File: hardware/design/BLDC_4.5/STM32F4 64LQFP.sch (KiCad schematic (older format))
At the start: 19 parts, among them P2 SWD, U1 STM32F40X_LQFP64, X2 8MHz 10ppm

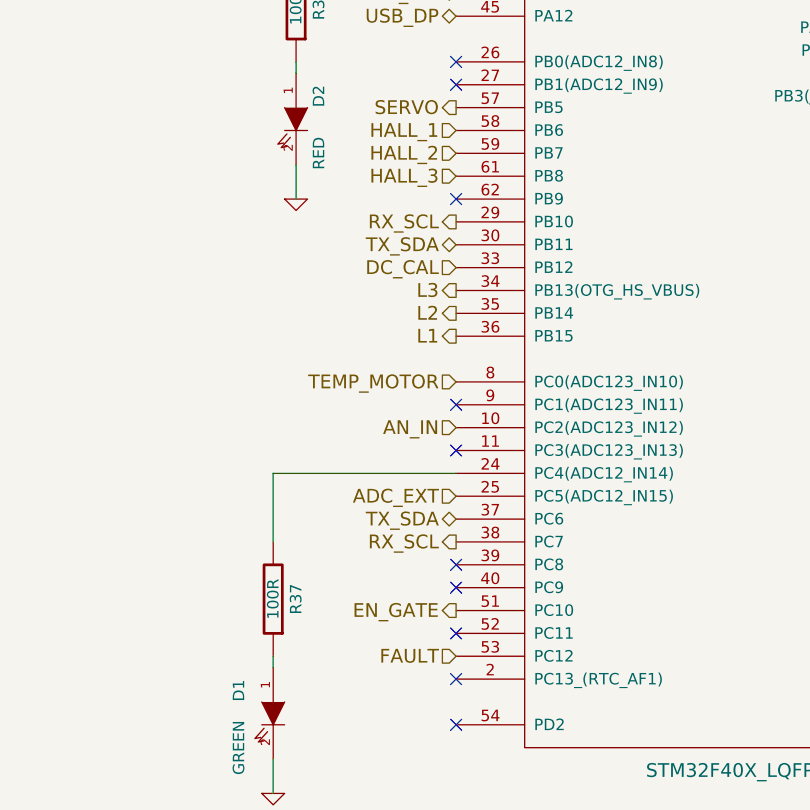
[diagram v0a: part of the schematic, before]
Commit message: Moved HALL_3 to PC11. Added CAN and I2C pullups and temperature sensor to the schematic.
Signed-off-by: Marcos Chaparro <marcos@mrkindustries.com.ar>
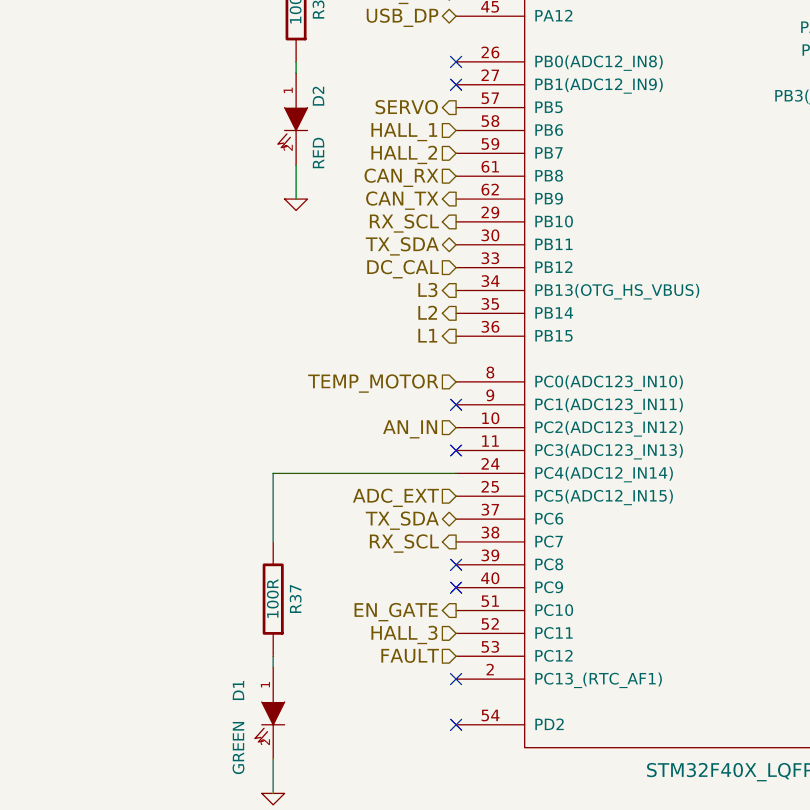
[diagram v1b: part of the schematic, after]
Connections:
- net HALL_3: now also U1.52 (PC11); no longer U1.61 (PB8)
- net CAN_TX: now reaches U1.62 (PB9)
- new net CAN_RX: U1.61 (PB8)
- no-connect marks 19 -> 17
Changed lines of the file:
@@
 LIBS:contrib
 LIBS:valves
+LIBS:mrk-industries
 LIBS:BLDC_4-cache
 EELAYER 24 0
@@
 $Descr A4 11693 8268
 encoding utf-8
-Sheet 3 4
+Sheet 4 6
 Title "BLDC Driver 4.5"
 Date "22 Aug 2014"
@@
 NoConn ~ 4500 5850
 NoConn ~ 4500 5350
-NoConn ~ 4500 3750
 NoConn ~ 4500 3250
 NoConn ~ 4500 3150
 NoConn ~ 4500 5450
-NoConn ~ 4500 5650
 $Comp
 L GND #PWR055
@@
 Text HLabel 4500 3550 0    60   Input ~ 0
 HALL_2
-Text HLabel 4500 3650 0    60   Input ~ 0
+Text HLabel 4500 5650 0    60   Input ~ 0
 HALL_3
 Text HLabel 4500 3850 0    60   Output ~ 0
@@
 Text Notes 9300 1700 0    40   ~ 0
 Bypass, place next to VDD pins
+Text HLabel 4500 3650 0    60   Input ~ 0
+CAN_RX
+Text HLabel 4500 3750 0    60   Output ~ 0
+CAN_TX
 $EndSCHEMATC

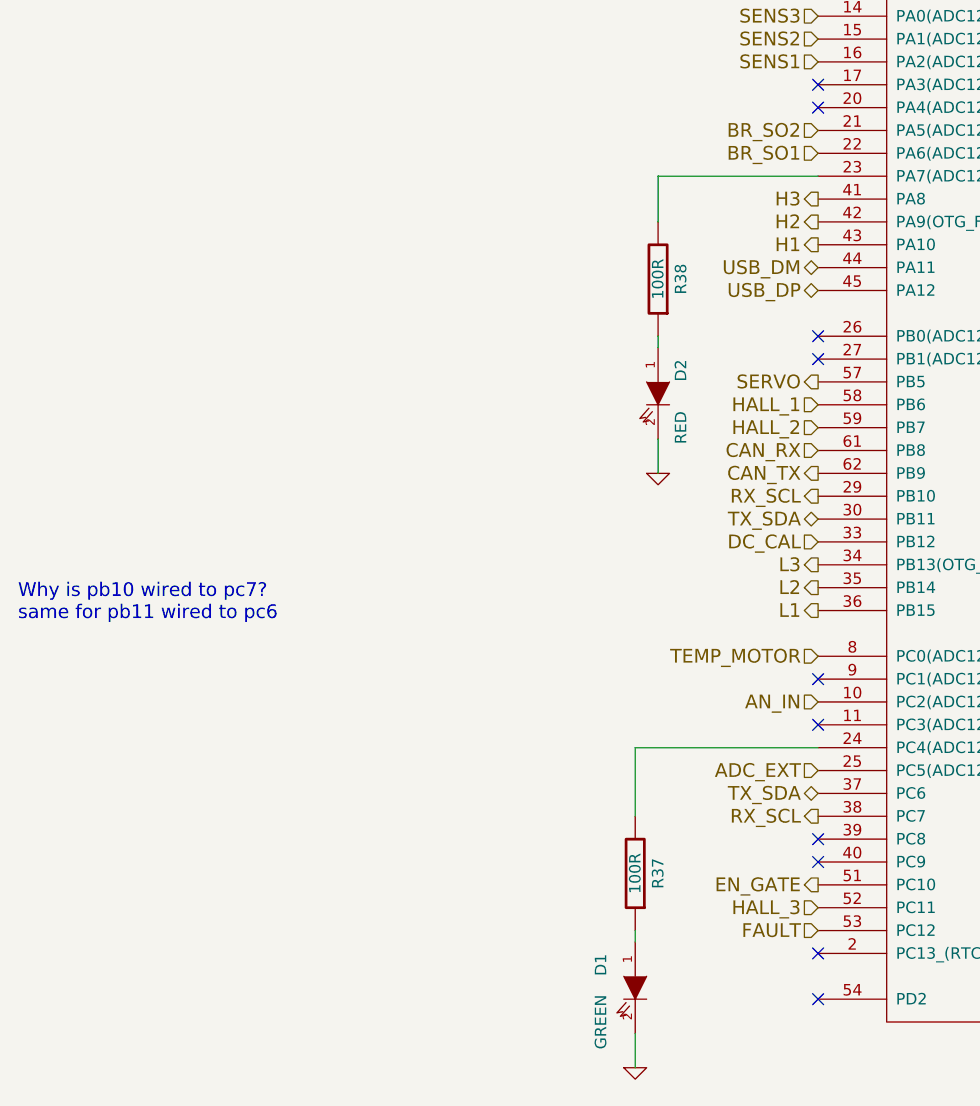
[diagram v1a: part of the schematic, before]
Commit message: Schematic changes: Cleaner top level, added CAN connector, moved LEDs to top level, added 22 Ohm resistors for the USB lines. Fully annotated schematic, ready for layout.
Signed-off-by: Marcos Chaparro <marcos@mrkindustries.com.ar>
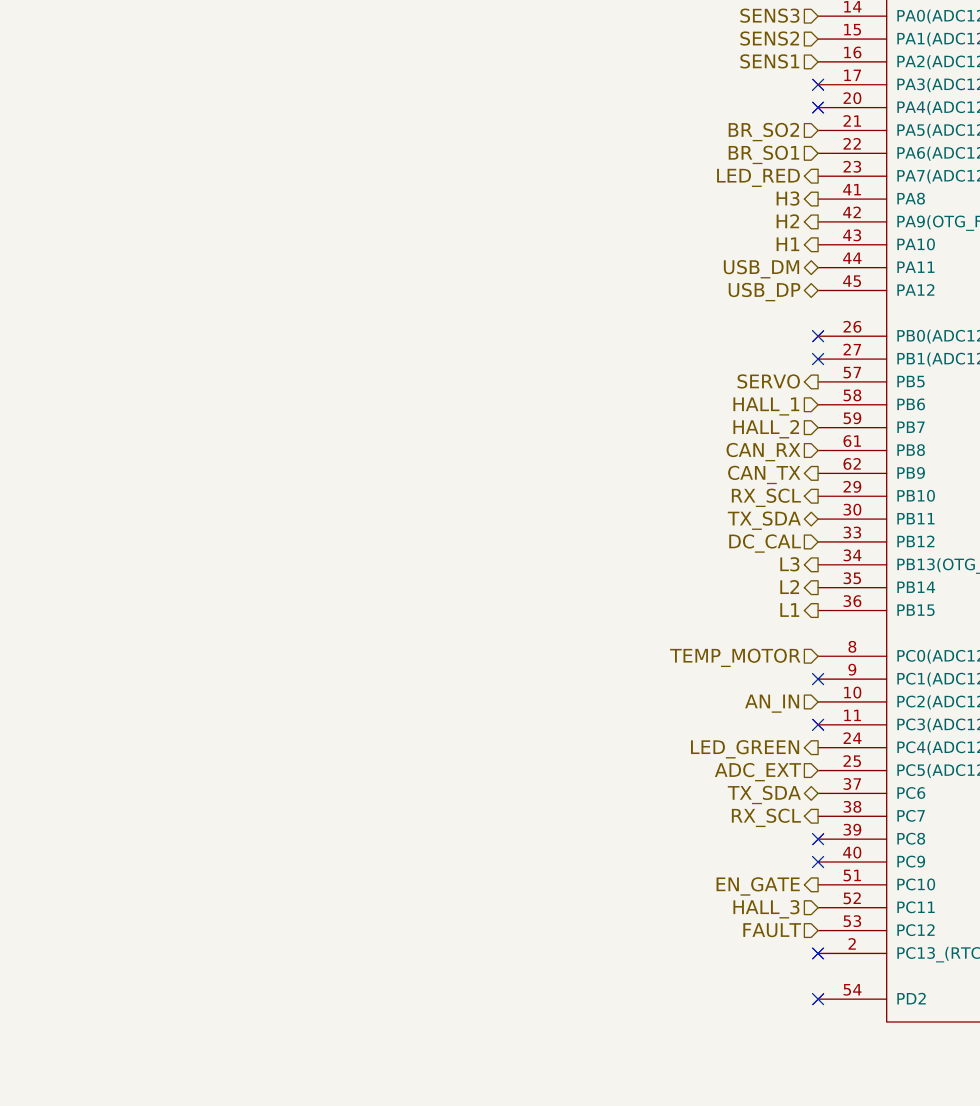
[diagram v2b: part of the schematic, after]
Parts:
- removed D1: GREEN, symbol LED
- removed D2: RED, symbol LED
- removed R37, R38: 100R, symbol R
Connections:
- net LED_RED: now reaches U1.23 (PA7(ADC12_IN7))
- net LED_GREEN: now reaches U1.24 (PC4(ADC12_IN14))
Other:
- note removed: "Why is pb10 wired to pc7?\nsame for pb11 wired to pc6"
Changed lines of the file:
@@
 LIBS:valves
 LIBS:mrk-industries
+LIBS:crf_1
 LIBS:BLDC_4-cache
 EELAYER 24 0
@@
 $Descr A4 11693 8268
 encoding utf-8
-Sheet 4 6
+Sheet 4 7
 Title "BLDC Driver 4.5"
-Date "22 Aug 2014"
+Date "25 Aug 2014"
 Rev "4.5"
 Comp "Benjamin Vedder"
@@
 $EndComp
 $Comp
-L GND #PWR047
+L GND #PWR607
 U 1 1 53F757BC
 P 8000 6050
-F 0 "#PWR047" H 8000 6050 30  0001 C CNN
+F 0 "#PWR607" H 8000 6050 30  0001 C CNN
 F 1 "GND" H 8000 5980 30  0001 C CNN
 F 2 "" H 8000 6050 60  0001 C CNN
@@
 $EndComp
 $Comp
-L VCC #PWR048
+L VCC #PWR605
 U 1 1 53F757C2
 P 7400 5100
-F 0 "#PWR048" H 7400 5200 30  0001 C CNN
+F 0 "#PWR605" H 7400 5200 30  0001 C CNN
 F 1 "VCC" H 7400 5200 30  0000 C CNN
 F 2 "" H 7400 5100 60  0001 C CNN
@@
 $EndComp
 $Comp
-L GND #PWR049
+L GND #PWR603
 U 1 1 53F757C8
 P 7200 5150
-F 0 "#PWR049" H 7200 5150 30  0001 C CNN
+F 0 "#PWR603" H 7200 5150 30  0001 C CNN
 F 1 "GND" H 7200 5080 30  0001 C CNN
 F 2 "" H 7200 5150 60  0001 C CNN
@@
 $EndComp
 $Comp
-L VCC #PWR050
+L VCC #PWR602
 U 1 1 53F757CE
 P 7200 4200
-F 0 "#PWR050" H 7200 4300 30  0001 C CNN
+F 0 "#PWR602" H 7200 4300 30  0001 C CNN
 F 1 "VCC" H 7200 4300 30  0000 C CNN
 F 2 "" H 7200 4200 60  0001 C CNN
@@
 $EndComp
 $Comp
-L GND #PWR051
+L GND #PWR608
 U 1 1 53F757E9
 P 8250 1600
-F 0 "#PWR051" H 8250 1600 30  0001 C CNN
+F 0 "#PWR608" H 8250 1600 30  0001 C CNN
 F 1 "GND" H 8250 1530 30  0001 C CNN
 F 2 "" H 8250 1600 60  0001 C CNN
@@
 $EndComp
 $Comp
-L GND #PWR052
+L GND #PWR601
 U 1 1 53F757EF
 P 7150 2550
-F 0 "#PWR052" H 7150 2550 30  0001 C CNN
+F 0 "#PWR601" H 7150 2550 30  0001 C CNN
 F 1 "GND" H 7150 2480 30  0001 C CNN
 F 2 "" H 7150 2550 60  0001 C CNN
@@
 NoConn ~ 7000 2450
 $Comp
-L VCC #PWR053
+L VCC #PWR604
 U 1 1 53F75807
 P 7200 5350
-F 0 "#PWR053" H 7200 5450 30  0001 C CNN
+F 0 "#PWR604" H 7200 5450 30  0001 C CNN
 F 1 "VCC" H 7200 5450 30  0000 C CNN
 F 2 "" H 7200 5350 60  0001 C CNN
@@
 NoConn ~ 7000 1850
 NoConn ~ 4500 2150
-$Comp
-L R R38
-U 1 1 53F75827
-P 3800 2900
-F 0 "R38" V 3700 2900 50  0000 C CNN
-F 1 "100R" V 3800 2900 50  0000 C CNN
-F 2 "" H 3800 2900 60  0001 C CNN
-F 3 "" H 3800 2900 60  0001 C CNN
-	1    3800 2900
-	-1   0    0    1
-$EndComp
-$Comp
-L R R37
-U 1 1 53F7582E
-P 3700 5500
-F 0 "R37" V 3600 5500 50  0000 C CNN
-F 1 "100R" V 3700 5500 50  0000 C CNN
-F 2 "" H 3700 5500 60  0001 C CNN
-F 3 "" H 3700 5500 60  0001 C CNN
-	1    3700 5500
-	-1   0    0    1
-$EndComp
-$Comp
-L LED D1
-U 1 1 53F75835
-P 3700 6000
-F 0 "D1" H 3600 5850 50  0000 C CNN
-F 1 "GREEN" H 3850 5850 50  0000 C CNN
-F 2 "" H 3700 6000 60  0001 C CNN
-F 3 "" H 3700 6000 60  0001 C CNN
-	1    3700 6000
-	0    1    1    0
-$EndComp
-$Comp
-L LED D2
-U 1 1 53F7583C
-P 3800 3400
-F 0 "D2" H 3700 3500 50  0000 C CNN
-F 1 "RED" H 3950 3500 50  0000 C CNN
-F 2 "" H 3800 3400 60  0001 C CNN
-F 3 "" H 3800 3400 60  0001 C CNN
-	1    3800 3400
-	0    1    1    0
-$EndComp
-$Comp
-L GND #PWR054
-U 1 1 53F75843
-P 3700 6350
-F 0 "#PWR054" H 3700 6350 30  0001 C CNN
-F 1 "GND" H 3700 6280 30  0001 C CNN
-F 2 "" H 3700 6350 60  0001 C CNN
-F 3 "" H 3700 6350 60  0001 C CNN
-	1    3700 6350
-	1    0    0    -1
-$EndComp
 NoConn ~ 4500 6050
 NoConn ~ 4500 5850
@@
 NoConn ~ 4500 5450
 $Comp
-L GND #PWR055
+L GND #PWR606
 U 1 1 53F75856
 P 7950 3300
-F 0 "#PWR055" H 7950 3300 30  0001 C CNN
+F 0 "#PWR606" H 7950 3300 30  0001 C CNN
 F 1 "GND" H 7950 3230 30  0001 C CNN
 F 2 "" H 7950 3300 60  0001 C CNN
@@
 	7950 3300 7950 3300
 Wire Wire Line
-	3700 4950 4500 4950
-Wire Wire Line
-	3700 5250 3700 4950
-Wire Wire Line
-	3800 2450 3800 2650
-Wire Wire Line
-	4500 2450 3800 2450
-Wire Wire Line
-	3800 3150 3800 3200
-Wire Wire Line
-	3700 5750 3700 5800
-Wire Wire Line
 	7200 5450 7200 5350
 Wire Wire Line
@@
 NoConn ~ 4500 4650
 NoConn ~ 4500 4850
-Wire Wire Line
-	3700 6200 3700 6350
-$Comp
-L GND #PWR056
-U 1 1 53F758A2
-P 3800 3750
-F 0 "#PWR056" H 3800 3750 30  0001 C CNN
-F 1 "GND" H 3800 3680 30  0001 C CNN
-F 2 "" H 3800 3750 60  0001 C CNN
-F 3 "" H 3800 3750 60  0001 C CNN
-	1    3800 3750
-	1    0    0    -1
-$EndComp
-Wire Wire Line
-	3800 3600 3800 3750
 $Comp
 L CONN_6 P2
@@
 $EndComp
 $Comp
-L VCC #PWR057
+L VCC #PWR612
 U 1 1 53F77417
 P 9900 2750
-F 0 "#PWR057" H 9900 2850 30  0001 C CNN
+F 0 "#PWR612" H 9900 2850 30  0001 C CNN
 F 1 "VCC" H 9900 2850 30  0000 C CNN
 F 2 "" H 9900 2750 60  0001 C CNN
@@
 $EndComp
 $Comp
-L GND #PWR058
+L GND #PWR611
 U 1 1 53F7741D
 P 9600 3100
-F 0 "#PWR058" H 9600 3100 30  0001 C CNN
+F 0 "#PWR611" H 9600 3100 30  0001 C CNN
 F 1 "GND" H 9600 3030 30  0001 C CNN
 F 2 "" H 9600 3100 60  0001 C CNN
@@
 $EndComp
 $Comp
-L GND #PWR059
+L GND #PWR610
 U 1 1 53F7743B
 P 9100 1650
-F 0 "#PWR059" H 9100 1650 30  0001 C CNN
+F 0 "#PWR610" H 9100 1650 30  0001 C CNN
 F 1 "GND" H 9100 1580 30  0001 C CNN
 F 2 "" H 9100 1650 60  0001 C CNN
@@
 $EndComp
 $Comp
-L VCC #PWR060
+L VCC #PWR609
 U 1 1 53F77441
 P 9100 950
-F 0 "#PWR060" H 9100 1050 30  0001 C CNN
+F 0 "#PWR609" H 9100 1050 30  0001 C CNN
 F 1 "VCC" H 9100 1050 30  0000 C CNN
 F 2 "" H 9100 950 60  0001 C CNN
@@
 Text HLabel 4500 5050 0    60   Input ~ 0
 ADC_EXT
-Text Notes 1000 4400 0    60   ~ 0
-Why is pb10 wired to pc7?\nsame for pb11 wired to pc6
 Text HLabel 4500 5150 0    60   3State ~ 0
 TX_SDA
@@
 Text HLabel 4500 3750 0    60   Output ~ 0
 CAN_TX
+Text HLabel 4500 2450 0    60   Output ~ 0
+LED_RED
+Text HLabel 4500 4950 0    60   Output ~ 0
+LED_GREEN
 $EndSCHEMATC

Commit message: Layout updated. Added inner power planes, changed USB connector, added CAN transceiver and connector, added 3D models copper pour under the mosfets and references moved to visible places
Signed-off-by: Marcos Chaparro <marcos@mrkindustries.com.ar>
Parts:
- C10, C11, C12, C13, C14, C15, C16, C17, C31, C32, C35, C38: footprint (none) -> SMD_Packages:SMD-0603_c
- P2: footprint (none) -> CRF1:MICRO_JST_6
- U1: footprint (none) -> CRF1:lqfp64_pad_mod
- X2: footprint (none) -> CRF1:Crystal_5x3mm
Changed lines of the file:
@@
 F 0 "U1" H 5700 6200 60  0000 C CNN
 F 1 "STM32F40X_LQFP64" H 5750 1550 60  0000 C CNN
-F 2 "" H 5750 3900 60  0001 C CNN
+F 2 "CRF1:lqfp64_pad_mod" H 5750 3900 60  0001 C CNN
 F 3 "" H 5750 3900 60  0001 C CNN
 	1    5750 3900
@@
 F 0 "C17" H 7550 6450 50  0000 L CNN
 F 1 "2.2u" H 7550 6250 50  0000 L CNN
-F 2 "" H 7500 6350 60  0001 C CNN
+F 2 "SMD_Packages:SMD-0603_c" H 7500 6350 60  0001 C CNN
 F 3 "" H 7500 6350 60  0001 C CNN
 	1    7500 6350
@@
 F 0 "C16" H 7550 6200 50  0000 L CNN
 F 1 "2.2u" H 7550 6000 50  0000 L CNN
-F 2 "" H 7500 6100 60  0001 C CNN
+F 2 "SMD_Packages:SMD-0603_c" H 7500 6100 60  0001 C CNN
 F 3 "" H 7500 6100 60  0001 C CNN
 	1    7500 6100
@@
 $EndComp
 $Comp
-L GND #PWR607
+L GND #PWR038
 U 1 1 53F757BC
 P 8000 6050
-F 0 "#PWR607" H 8000 6050 30  0001 C CNN
+F 0 "#PWR038" H 8000 6050 30  0001 C CNN
 F 1 "GND" H 8000 5980 30  0001 C CNN
 F 2 "" H 8000 6050 60  0001 C CNN
@@
 $EndComp
 $Comp
-L VCC #PWR605
+L VCC #PWR039
 U 1 1 53F757C2
 P 7400 5100
-F 0 "#PWR605" H 7400 5200 30  0001 C CNN
+F 0 "#PWR039" H 7400 5200 30  0001 C CNN
 F 1 "VCC" H 7400 5200 30  0000 C CNN
 F 2 "" H 7400 5100 60  0001 C CNN
@@
 $EndComp
 $Comp
-L GND #PWR603
+L GND #PWR040
 U 1 1 53F757C8
 P 7200 5150
-F 0 "#PWR603" H 7200 5150 30  0001 C CNN
+F 0 "#PWR040" H 7200 5150 30  0001 C CNN
 F 1 "GND" H 7200 5080 30  0001 C CNN
 F 2 "" H 7200 5150 60  0001 C CNN
@@
 $EndComp
 $Comp
-L VCC #PWR602
+L VCC #PWR041
 U 1 1 53F757CE
 P 7200 4200
-F 0 "#PWR602" H 7200 4300 30  0001 C CNN
+F 0 "#PWR041" H 7200 4300 30  0001 C CNN
 F 1 "VCC" H 7200 4300 30  0000 C CNN
 F 2 "" H 7200 4200 60  0001 C CNN
@@
 F 0 "X2" H 7750 2200 60  0000 C CNN
 F 1 "8MHz 10ppm" H 7750 1900 60  0000 C CNN
-F 2 "" H 7750 2050 60  0001 C CNN
+F 2 "CRF1:Crystal_5x3mm" H 7750 2050 60  0001 C CNN
 F 3 "" H 7750 2050 60  0001 C CNN
 F 4 "ABM3B-8.0-10-1UT" H 7750 2050 60  0001 C CNN "mfg#"
@@
 F 0 "C15" H 7400 1900 50  0000 L CNN
 F 1 "15p" H 7400 1700 50  0000 L CNN
-F 2 "" H 7350 1800 60  0001 C CNN
+F 2 "SMD_Packages:SMD-0603_c" H 7350 1800 60  0001 C CNN
 F 3 "" H 7350 1800 60  0001 C CNN
 	1    7350 1800
@@
 F 0 "C38" H 8150 1900 50  0000 L CNN
 F 1 "15p" H 8150 1700 50  0000 L CNN
-F 2 "" H 8100 1800 60  0001 C CNN
+F 2 "SMD_Packages:SMD-0603_c" H 8100 1800 60  0001 C CNN
 F 3 "" H 8100 1800 60  0001 C CNN
 	1    8100 1800
@@
 $EndComp
 $Comp
-L GND #PWR608
+L GND #PWR042
 U 1 1 53F757E9
 P 8250 1600
-F 0 "#PWR608" H 8250 1600 30  0001 C CNN
+F 0 "#PWR042" H 8250 1600 30  0001 C CNN
 F 1 "GND" H 8250 1530 30  0001 C CNN
 F 2 "" H 8250 1600 60  0001 C CNN
@@
 $EndComp
 $Comp
-L GND #PWR601
+L GND #PWR043
 U 1 1 53F757EF
 P 7150 2550
-F 0 "#PWR601" H 7150 2550 30  0001 C CNN
+F 0 "#PWR043" H 7150 2550 30  0001 C CNN
 F 1 "GND" H 7150 2480 30  0001 C CNN
 F 2 "" H 7150 2550 60  0001 C CNN
@@
 F 0 "C31" H 7800 5550 50  0000 L CNN
 F 1 "2.2u" H 7800 5350 50  0000 L CNN
-F 2 "" H 7750 5450 60  0001 C CNN
+F 2 "SMD_Packages:SMD-0603_c" H 7750 5450 60  0001 C CNN
 F 3 "" H 7750 5450 60  0001 C CNN
 	1    7750 5450
@@
 F 0 "C35" H 8050 5550 50  0000 L CNN
 F 1 "2.2u" H 8050 5350 50  0000 L CNN
-F 2 "" H 8000 5450 60  0001 C CNN
+F 2 "SMD_Packages:SMD-0603_c" H 8000 5450 60  0001 C CNN
 F 3 "" H 8000 5450 60  0001 C CNN
 	1    8000 5450
@@
 NoConn ~ 7000 2450
 $Comp
-L VCC #PWR604
+L VCC #PWR044
 U 1 1 53F75807
 P 7200 5350
-F 0 "#PWR604" H 7200 5450 30  0001 C CNN
+F 0 "#PWR044" H 7200 5450 30  0001 C CNN
 F 1 "VCC" H 7200 5450 30  0000 C CNN
 F 2 "" H 7200 5350 60  0001 C CNN
@@
 NoConn ~ 4500 5450
 $Comp
-L GND #PWR606
+L GND #PWR045
 U 1 1 53F75856
 P 7950 3300
-F 0 "#PWR606" H 7950 3300 30  0001 C CNN
+F 0 "#PWR045" H 7950 3300 30  0001 C CNN
 F 1 "GND" H 7950 3230 30  0001 C CNN
 F 2 "" H 7950 3300 60  0001 C CNN
@@
 F 0 "C32" H 8000 3200 50  0000 L CNN
 F 1 "100n" H 8000 3000 50  0000 L CNN
-F 2 "" H 7950 3100 60  0001 C CNN
+F 2 "SMD_Packages:SMD-0603_c" H 7950 3100 60  0001 C CNN
 F 3 "" H 7950 3100 60  0001 C CNN
 	1    7950 3100
@@
 F 0 "P2" V 10050 3150 60  0000 C CNN
 F 1 "SWD" V 10150 3150 60  0000 C CNN
-F 2 "" H 10100 3150 60  0001 C CNN
+F 2 "CRF1:MICRO_JST_6" H 10100 3150 60  0001 C CNN
 F 3 "" H 10100 3150 60  0001 C CNN
 	1    10100 3150
@@
 $EndComp
 $Comp
-L VCC #PWR612
+L VCC #PWR046
 U 1 1 53F77417
 P 9900 2750
-F 0 "#PWR612" H 9900 2850 30  0001 C CNN
+F 0 "#PWR046" H 9900 2850 30  0001 C CNN
 F 1 "VCC" H 9900 2850 30  0000 C CNN
 F 2 "" H 9900 2750 60  0001 C CNN
@@
 $EndComp
 $Comp
-L GND #PWR611
+L GND #PWR047
 U 1 1 53F7741D
 P 9600 3100
-F 0 "#PWR611" H 9600 3100 30  0001 C CNN
+F 0 "#PWR047" H 9600 3100 30  0001 C CNN
 F 1 "GND" H 9600 3030 30  0001 C CNN
 F 2 "" H 9600 3100 60  0001 C CNN
@@
 F 0 "C10" H 9450 1400 50  0000 L CNN
 F 1 "2.2u" H 9450 1200 50  0000 L CNN
-F 2 "" H 9400 1300 60  0001 C CNN
+F 2 "SMD_Packages:SMD-0603_c" H 9400 1300 60  0001 C CNN
 F 3 "" H 9400 1300 60  0001 C CNN
 	1    9400 1300
@@
 F 0 "C11" H 9700 1400 50  0000 L CNN
 F 1 "2.2u" H 9700 1200 50  0000 L CNN
-F 2 "" H 9650 1300 60  0001 C CNN
+F 2 "SMD_Packages:SMD-0603_c" H 9650 1300 60  0001 C CNN
 F 3 "" H 9650 1300 60  0001 C CNN
 	1    9650 1300
@@
 F 0 "C14" H 10450 1400 50  0000 L CNN
 F 1 "2.2u" H 10450 1200 50  0000 L CNN
-F 2 "" H 10400 1300 60  0001 C CNN
+F 2 "SMD_Packages:SMD-0603_c" H 10400 1300 60  0001 C CNN
 F 3 "" H 10400 1300 60  0001 C CNN
 	1    10400 1300
@@
 $EndComp
 $Comp
-L GND #PWR610
+L GND #PWR048
 U 1 1 53F7743B
 P 9100 1650
-F 0 "#PWR610" H 9100 1650 30  0001 C CNN
+F 0 "#PWR048" H 9100 1650 30  0001 C CNN
 F 1 "GND" H 9100 1580 30  0001 C CNN
 F 2 "" H 9100 1650 60  0001 C CNN
@@
 $EndComp
 $Comp
-L VCC #PWR609
+L VCC #PWR049
 U 1 1 53F77441
 P 9100 950
-F 0 "#PWR609" H 9100 1050 30  0001 C CNN
+F 0 "#PWR049" H 9100 1050 30  0001 C CNN
 F 1 "VCC" H 9100 1050 30  0000 C CNN
 F 2 "" H 9100 950 60  0001 C CNN
@@
 F 0 "C12" H 9950 1400 50  0000 L CNN
 F 1 "2.2u" H 9950 1200 50  0000 L CNN
-F 2 "" H 9900 1300 60  0001 C CNN
+F 2 "SMD_Packages:SMD-0603_c" H 9900 1300 60  0001 C CNN
 F 3 "" H 9900 1300 60  0001 C CNN
 	1    9900 1300
@@
 F 0 "C13" H 10200 1400 50  0000 L CNN
 F 1 "2.2u" H 10200 1200 50  0000 L CNN
-F 2 "" H 10150 1300 60  0001 C CNN
+F 2 "SMD_Packages:SMD-0603_c" H 10150 1300 60  0001 C CNN
 F 3 "" H 10150 1300 60  0001 C CNN
 	1    10150 1300
@@
 $Bitmap
 Pos 1750 6700
-Scale 1.000000
+Scale 1,000000
 Data
 89 50 4E 47 0D 0A 1A 0A 00 00 00 0D 49 48 44 52 00 00 02 6A 00 00 02 41 08 02 00 00 00 79 DB 0E
@@
 $Bitmap
 Pos 3100 1050
-Scale 1.500000
+Scale 1,000000
 Data
 89 50 4E 47 0D 0A 1A 0A 00 00 00 0D 49 48 44 52 00 00 03 D4 00 00 00 CC 08 02 00 00 00 1D DB 7C
